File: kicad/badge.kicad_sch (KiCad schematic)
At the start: 36 parts, among them U1 ATtiny85-20P, U2 4021, U3 74HC595, U4 74HC595

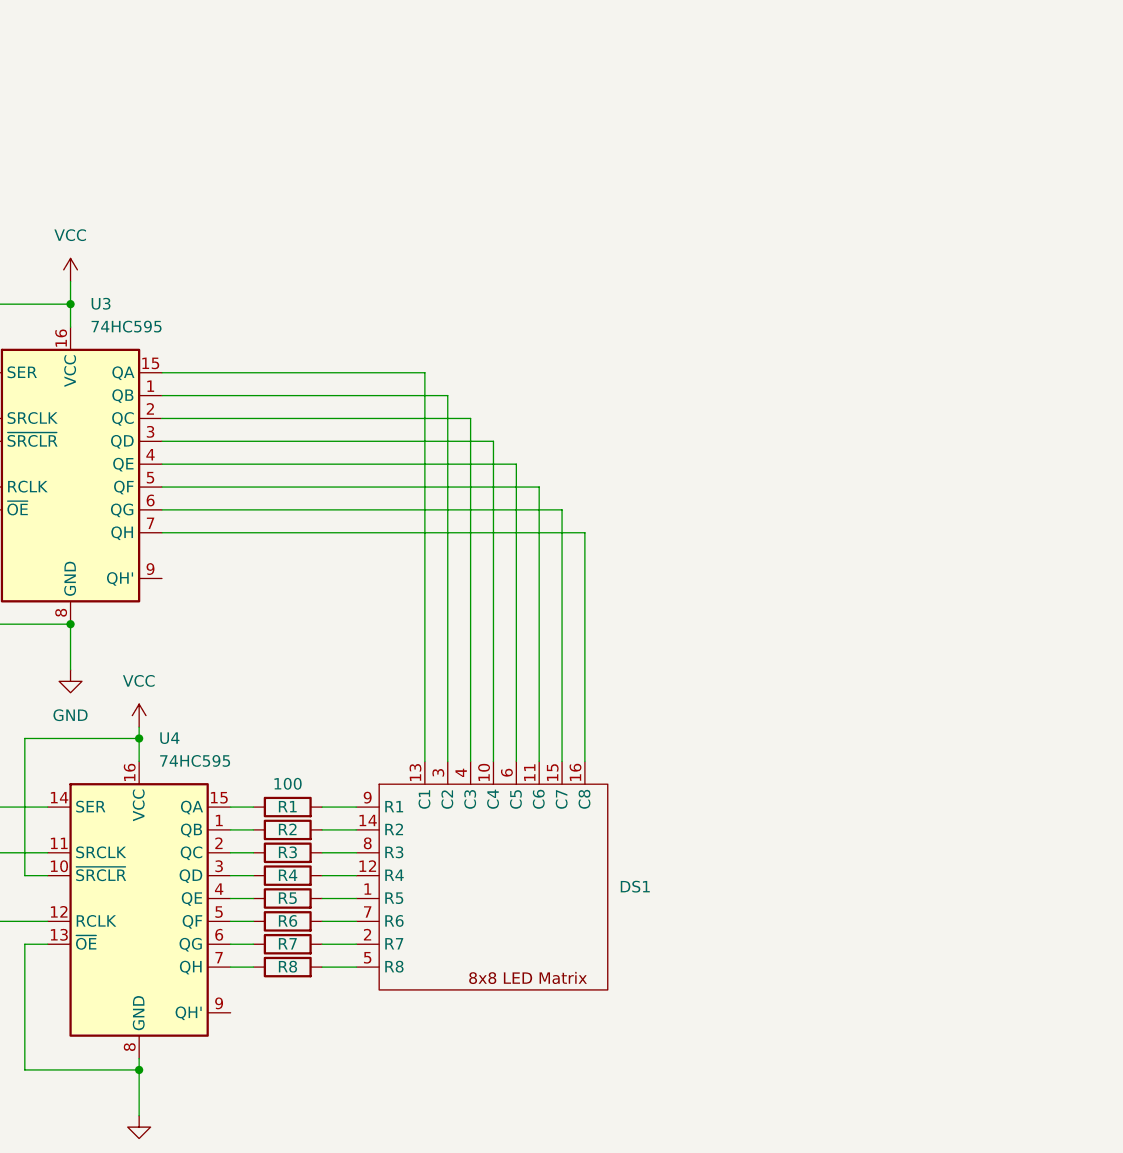
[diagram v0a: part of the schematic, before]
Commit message: Add surface mount parts
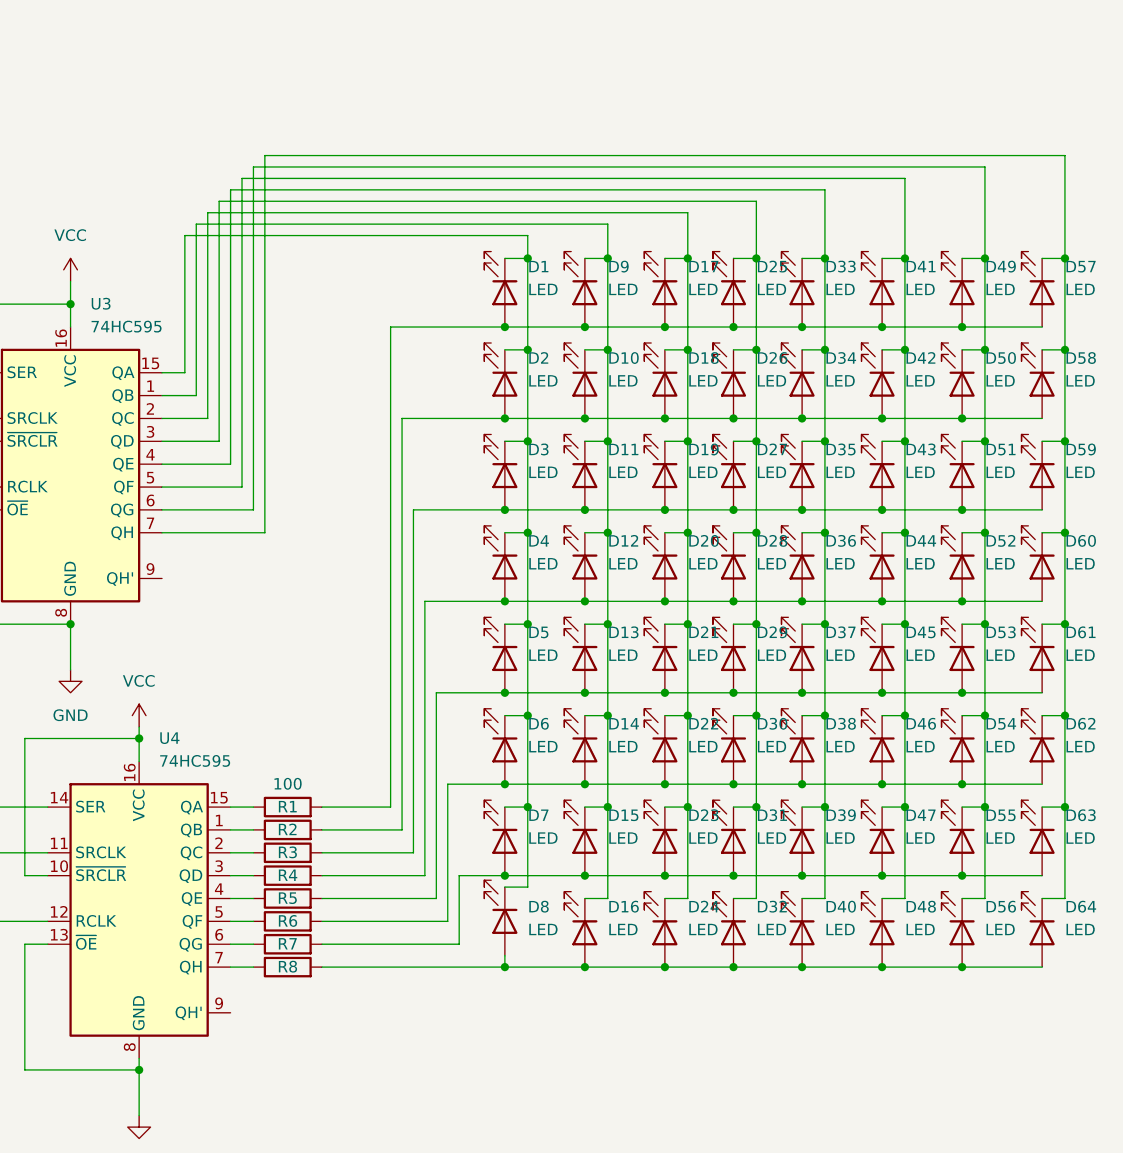
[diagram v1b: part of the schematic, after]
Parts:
- removed DS1: ~, badge:8x8 LED Matrix, symbol badge_library:8x8_LED_Matrix
- added D1, D10, D11, D12, D13, D14, D15, D16, D17, D18, D19, D2, D20, D21, D22, D23, D24, D25, D26, D27, D28, D29, D3, D30, D31, D32, D33, D34, D35, D36, D37, D38, D39, D4, D40, D41, D42, D43, D44, D45, D46, D47, D48, D49, D5, D50, D51, D52, D53, D54, D55, D56, D57, D58, D59, D6, D60, D61, D62, D63, D64, D7, D8, D9: LED, LED_SMD:LED_1206_3216Metric_Pad1.42x1.75mm_HandSolder, symbol Device:LED
- R1, R10, R11, R12, R13, R14, R15, R16, R2, R3, R4, R5, R6, R7, R8, R9: footprint Resistor_THT:R_Axial_DIN0207_L6.3mm_D2.5mm_P10.16mm_Horizontal -> Resistor_SMD:R_1206_3216Metric_Pad1.30x1.75mm_HandSolder
- S1, S2, S3, S4, S5, S6: footprint badge:button -> badge-footprints:button
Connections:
- net at R1.2: now also D1.2 (A), D17.2 (A), D25.2 (A), D33.2 (A), D41.2 (A), D49.2 (A), D57.2 (A), D9.2 (A)
- net at R4.2: now also D12.2 (A), D20.2 (A), D28.2 (A), D36.2 (A), D4.2 (A), D44.2 (A), D52.2 (A), D60.2 (A)
- net at R2.2: now also D10.2 (A), D18.2 (A), D2.2 (A), D26.2 (A), D34.2 (A), D42.2 (A), D50.2 (A), D58.2 (A)
- net at R6.2: now also D14.2 (A), D22.2 (A), D30.2 (A), D38.2 (A), D46.2 (A), D54.2 (A), D6.2 (A), D62.2 (A)
- net at R8.2: now also D16.2 (A), D24.2 (A), D32.2 (A), D40.2 (A), D48.2 (A), D56.2 (A), D64.2 (A), D8.2 (A)
- net at R7.2: now also D15.2 (A), D23.2 (A), D31.2 (A), D39.2 (A), D47.2 (A), D55.2 (A), D63.2 (A), D7.2 (A)
- net at U3.1 (QB): now also D10.1 (K), D11.1 (K), D12.1 (K), D13.1 (K), D14.1 (K), D15.1 (K), D16.1 (K), D9.1 (K)
- net at U3.15 (QA): now also D1.1 (K), D2.1 (K), D3.1 (K), D4.1 (K), D5.1 (K), D6.1 (K), D7.1 (K), D8.1 (K)
- net at U3.2 (QC): now also D17.1 (K), D18.1 (K), D19.1 (K), D20.1 (K), D21.1 (K), D22.1 (K), D23.1 (K), D24.1 (K)
- net at U3.3 (QD): now also D25.1 (K), D26.1 (K), D27.1 (K), D28.1 (K), D29.1 (K), D30.1 (K), D31.1 (K), D32.1 (K)
- net at U3.4 (QE): now also D33.1 (K), D34.1 (K), D35.1 (K), D36.1 (K), D37.1 (K), D38.1 (K), D39.1 (K), D40.1 (K)
- net at U3.5 (QF): now also D41.1 (K), D42.1 (K), D43.1 (K), D44.1 (K), D45.1 (K), D46.1 (K), D47.1 (K), D48.1 (K)
- net at U3.6 (QG): now also D49.1 (K), D50.1 (K), D51.1 (K), D52.1 (K), D53.1 (K), D54.1 (K), D55.1 (K), D56.1 (K)
- net at U3.7 (QH): now also D57.1 (K), D58.1 (K), D59.1 (K), D60.1 (K), D61.1 (K), D62.1 (K), D63.1 (K), D64.1 (K)
- net at R3.2: now also D11.2 (A), D19.2 (A), D27.2 (A), D3.2 (A), D35.2 (A), D43.2 (A), D51.2 (A), D59.2 (A)
- net at R5.2: now also D13.2 (A), D21.2 (A), D29.2 (A), D37.2 (A), D45.2 (A), D5.2 (A), D53.2 (A), D61.2 (A)

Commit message: Update surface mount badge
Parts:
- BAT1: value BS-7 -> CR2032; footprint digikey-footprints:Battery_Holder_Coin_2032_BS-7 -> Battery:BatteryHolder_MPD_BC2003_1x2032; JLCPCB Part # (none) -> C70373
- R1, R10, R11, R12, R13, R14, R15, R16, R2, R3, R4, R5, R6, R7, R8, R9: footprint Resistor_SMD:R_1206_3216Metric_Pad1.30x1.75mm_HandSolder -> PCM_JLCPCB:R_0805
- S1: value TL3315NF160Q -> C83206; footprint badge-footprints:button -> Button_Switch_SMD:SW_MEC_5GSH9; Category Switches -> (none); DK_Datasheet_Link http://spec_sheets.e-switch.com/specs/P010337.pdf -> (none); DK_Detail_Page /product-detail/en/e-switch/TL3315NF160Q/EG4621CT-ND/1870401 -> (none); Digi-Key_PN EG4621CT-ND -> (none); Family Tactile Switches -> (none); MPN TL3315NF160Q -> (none); Manufacturer E-Switch -> (none); Status Active -> (none)
- S2, S3, S4, S5, S6: value TL3315NF160Q -> C83206; footprint badge-footprints:button -> Badge-Library:C83206
- U1: value ATtiny85-20P -> ATtiny85-20SF; footprint Package_DIP:DIP-8_W7.62mm -> Package_SO:SOIC-8_5.3x5.3mm_P1.27mm; JLCPCB Part # (none) -> C615549
- U2: value 4021 -> CD4021B; footprint Package_DIP:DIP-16_W7.62mm -> PCM_JLCPCB:SOIC-16_L9.9-W3.9-P1.27-LS6.0-BL; JLCPCB Part # (none) -> C6729
- U3, U4: value 74HC595 -> SN74HC595; footprint Package_DIP:DIP-16_W7.62mm -> PCM_JLCPCB:SOIC-16_L9.9-W3.9-P1.27-LS6.0-BL; JLCPCB Part # (none) -> C5947
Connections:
- net GND: now also BAT1.2; no longer BAT1.Neg
- net VCC: now also BAT1.1; no longer BAT1.Pos

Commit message: Update labels
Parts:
- BAT1: JLCPCB Part # C70373 -> C964831
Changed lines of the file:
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@@
 			)
 		)
-		(property "JLCPCB Part #" "C70373"
+		(property "JLCPCB Part #" "C964831"
 			(at 30.48 166.37 0)
 			(effects
